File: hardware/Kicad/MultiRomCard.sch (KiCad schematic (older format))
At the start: 16 parts, among them P1 VC4000_Cartridge_Bus, U1 Arduino_UNO, U2 74HC595, U3 74HC595, U4 74HC595, U5 6264, U6 74HC245, U7 74HC245, U8 74HC245

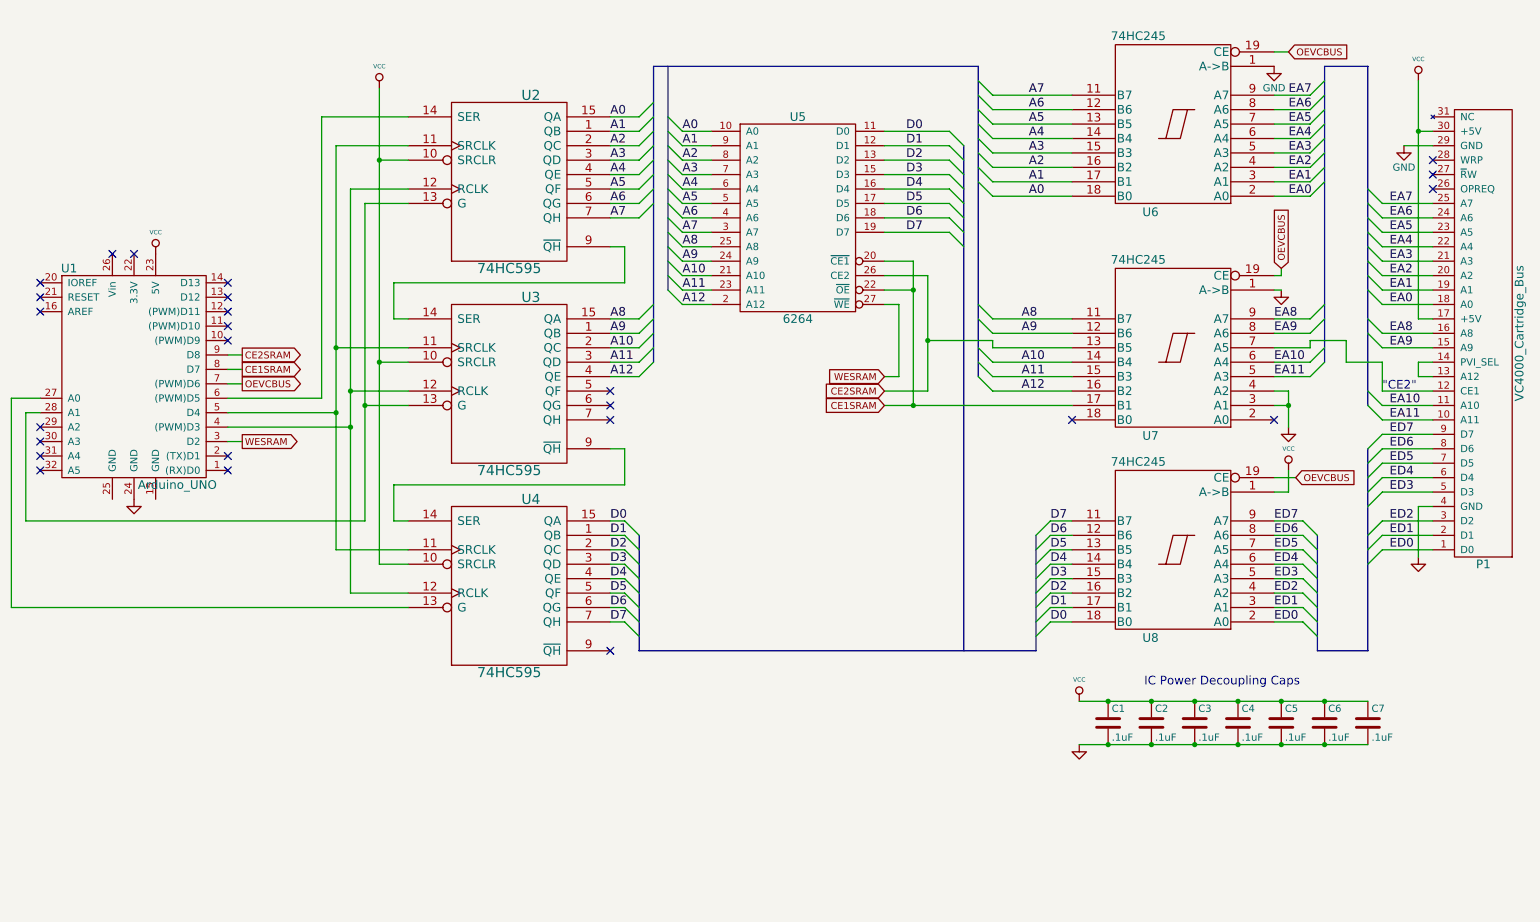
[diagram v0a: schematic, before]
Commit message: [SCH/PCB] Added and connected missing Arduino GND Pins.
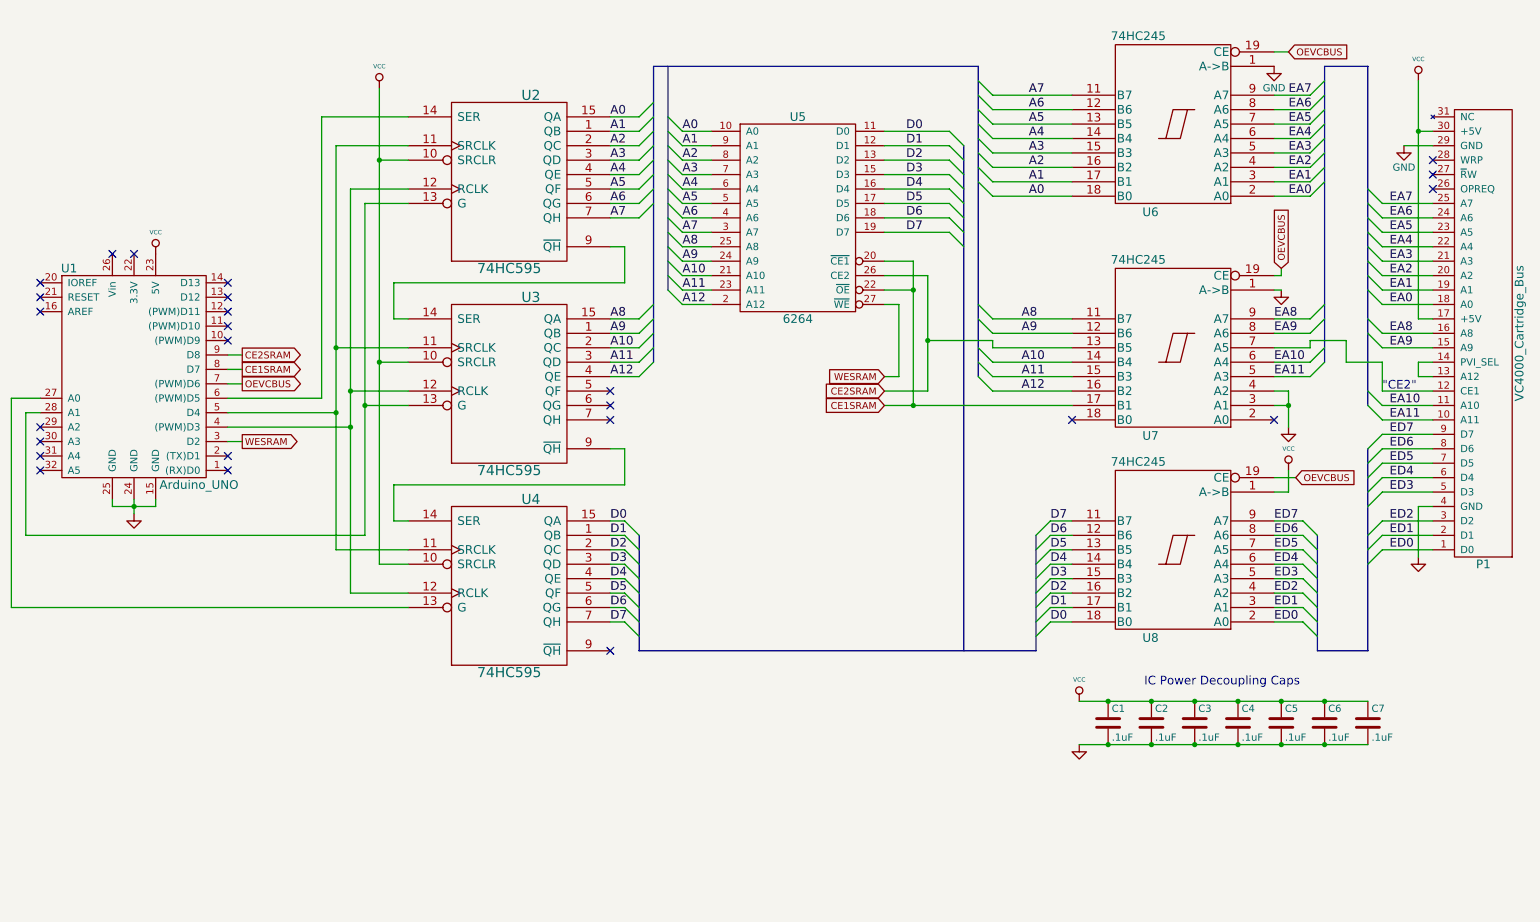
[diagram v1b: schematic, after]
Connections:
- net GND: now also U1.15 (GND), U1.25 (GND)

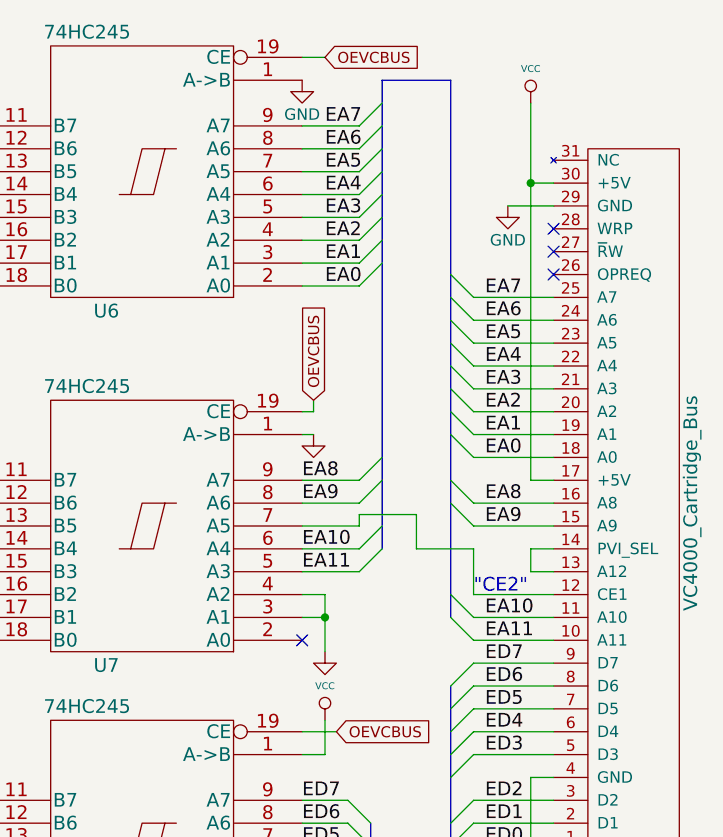
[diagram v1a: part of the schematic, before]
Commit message: [SCH/PCB] Cleaning up both schematic and PCB a bit.
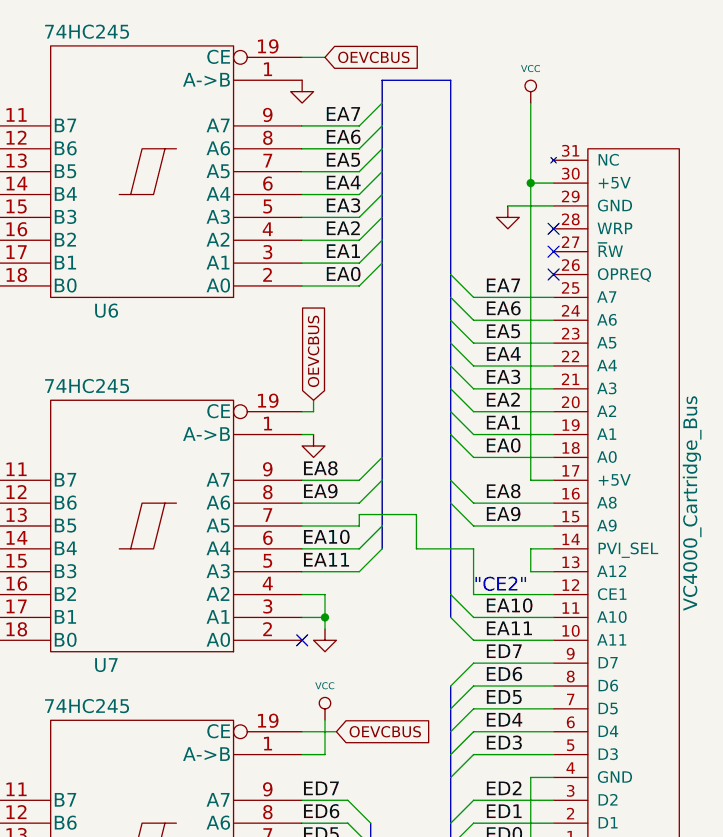
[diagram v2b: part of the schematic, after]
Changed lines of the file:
@@
 Sheet 1 1
 Title "Interton VC4000 MultiRom Cartridge"
-Date "Sunday, June 21, 2015"
+Date "Monday, June 22, 2015"
 Rev "0.1"
 Comp "Mario Keller and Johannes Maibaum"
@@
 L GND #PWR07
 U 1 1 54DB8BDD
-P 9550 4000
-F 0 "#PWR07" H 9550 4000 30  0001 C CNN
-F 1 "GND" H 9550 3930 30  0001 C CNN
-F 2 "" H 9550 4000 60  0000 C CNN
-F 3 "" H 9550 4000 60  0000 C CNN
-	1    9550 4000
+P 9550 3900
+F 0 "#PWR07" H 9550 3900 30  0001 C CNN
+F 1 "GND" H 9550 3830 30  0001 C CNN
+F 2 "" H 9550 3900 60  0000 C CNN
+F 3 "" H 9550 3900 60  0000 C CNN
+	1    9550 3900
 	1    0    0    -1
 $EndComp
@@
 Text Notes 10200 3750 0    60   ~ 0
 "CE2"
-$Comp
-L GND #PWR09
-U 1 1 553D09E4
-P 10350 2050
-F 0 "#PWR09" H 10350 1800 50  0001 C CNN
-F 1 "GND" H 10350 1900 50  0000 C CNN
-F 2 "" H 10350 2050 60  0000 C CNN
-F 3 "" H 10350 2050 60  0000 C CNN
-	1    10350 2050
-	1    0    0    -1
-$EndComp
-$Comp
-L GND #PWR010
-U 1 1 553D11BE
-P 9450 1500
-F 0 "#PWR010" H 9450 1250 50  0001 C CNN
-F 1 "GND" H 9450 1350 50  0000 C CNN
-F 2 "" H 9450 1500 60  0000 C CNN
-F 3 "" H 9450 1500 60  0000 C CNN
-	1    9450 1500
-	1    0    0    -1
-$EndComp
 Entry Wire Line
 	10100 4750 10200 4650
@@
 $EndComp
 $Comp
-L GND #PWR011
+L GND #PWR09
 U 1 1 558564D3
 P 8100 6200
-F 0 "#PWR011" H 8100 6200 30  0001 C CNN
+F 0 "#PWR09" H 8100 6200 30  0001 C CNN
 F 1 "GND" H 8100 6130 30  0001 C CNN
 F 2 "" H 8100 6200 60  0000 C CNN
@@
 $EndComp
 $Comp
-L VCC #PWR012
+L VCC #PWR010
 U 1 1 5585650E
 P 8100 5900
-F 0 "#PWR012" H 8100 6000 30  0001 C CNN
+F 0 "#PWR010" H 8100 6000 30  0001 C CNN
 F 1 "VCC" H 8100 6050 30  0000 C CNN
 F 2 "" H 8100 5900 60  0000 C CNN
@@
 	6750 3850 8050 3850
 Wire Wire Line
-	9550 3750 9550 4000
+	9550 3750 9550 3900
 Wire Wire Line
 	9550 3850 9450 3850
@@
 	1700 4550 1700 4500
 Connection ~ 1550 4550
+$Comp
+L GND #PWR011
+U 1 1 5587E073
+P 9450 1500
+F 0 "#PWR011" H 9450 1500 30  0001 C CNN
+F 1 "GND" H 9450 1430 30  0001 C CNN
+F 2 "" H 9450 1500 60  0000 C CNN
+F 3 "" H 9450 1500 60  0000 C CNN
+	1    9450 1500
+	1    0    0    -1
+$EndComp
+$Comp
+L GND #PWR012
+U 1 1 5587E24F
+P 10350 2050
+F 0 "#PWR012" H 10350 2050 30  0001 C CNN
+F 1 "GND" H 10350 1980 30  0001 C CNN
+F 2 "" H 10350 2050 60  0000 C CNN
+F 3 "" H 10350 2050 60  0000 C CNN
+	1    10350 2050
+	1    0    0    -1
+$EndComp
 $EndSCHEMATC

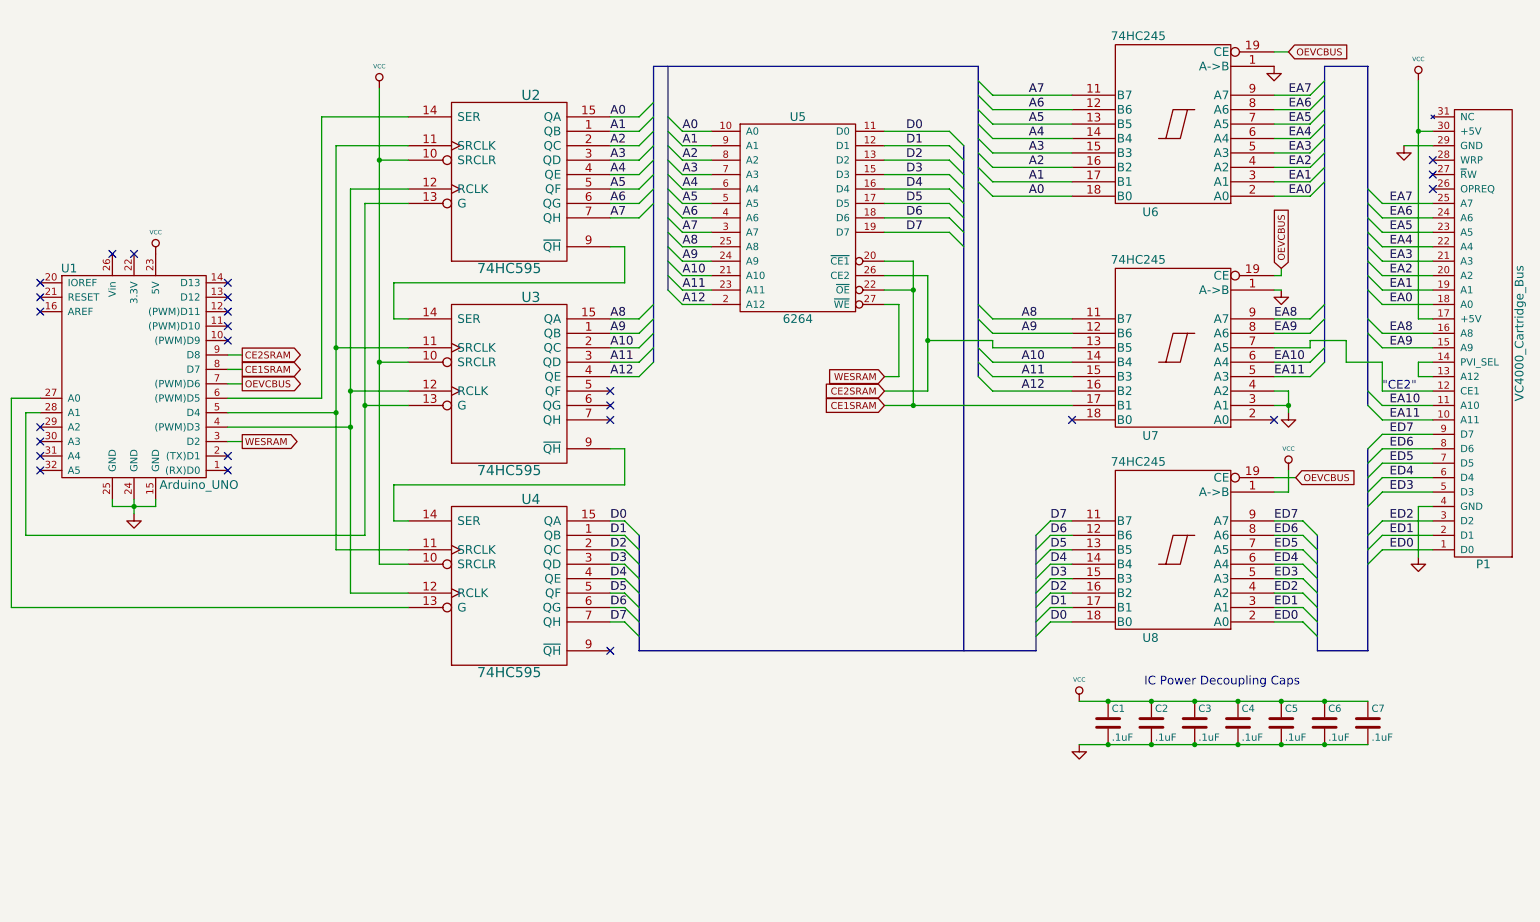
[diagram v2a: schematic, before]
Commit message: [SCH/PCB] Add Pin header for MicroSD Card Breakout Board.
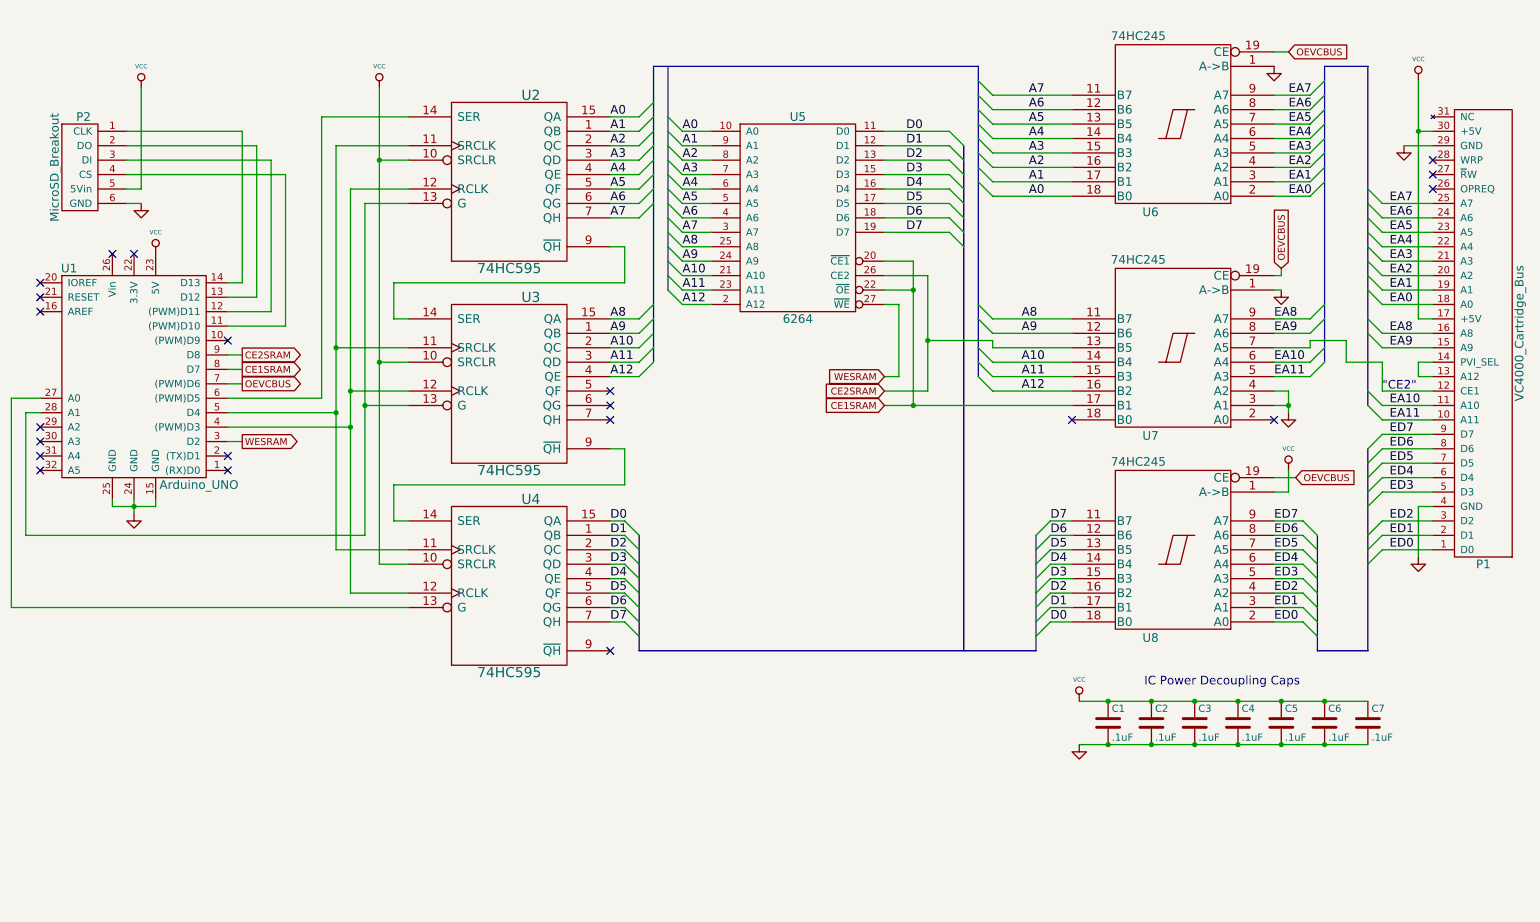
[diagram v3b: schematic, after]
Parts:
- added P2: MicroSD_Breakout, Pin_Headers:Pin_Header_Straight_1x06, symbol MicroSD_Breakout
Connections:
- net GND: now also P2.6 (GND)
- net VCC: now also P2.5 (5Vin)
- net at U1.11 ((PWM)D10): now also P2.4 (CS)
- net at U1.12 ((PWM)D11): now also P2.3 (DI)
- net at U1.13 (D12): now also P2.2 (DO)
- net at U1.14 (D13): now also P2.1 (CLK)
- no-connect marks 25 -> 21
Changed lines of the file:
@@
 NoConn ~ 2200 4300
 NoConn ~ 2200 4200
-NoConn ~ 2200 3400
-NoConn ~ 2200 3300
-NoConn ~ 2200 3200
-NoConn ~ 2200 3100
-NoConn ~ 2200 3000
 $Comp
 L VCC #PWR03
@@
 Text Notes 8550 5800 0    60   ~ 0
 IC Power Decoupling Caps
+$Comp
+L GND #PWR011
+U 1 1 5587E073
+P 9450 1500
+F 0 "#PWR011" H 9450 1500 30  0001 C CNN
+F 1 "GND" H 9450 1430 30  0001 C CNN
+F 2 "" H 9450 1500 60  0000 C CNN
+F 3 "" H 9450 1500 60  0000 C CNN
+	1    9450 1500
+	1    0    0    -1
+$EndComp
+$Comp
+L GND #PWR012
+U 1 1 5587E24F
+P 10350 2050
+F 0 "#PWR012" H 10350 2050 30  0001 C CNN
+F 1 "GND" H 10350 1980 30  0001 C CNN
+F 2 "" H 10350 2050 60  0000 C CNN
+F 3 "" H 10350 2050 60  0000 C CNN
+	1    10350 2050
+	1    0    0    -1
+$EndComp
+$Comp
+L GND #PWR013
+U 1 1 5587EA58
+P 1600 2450
+F 0 "#PWR013" H 1600 2450 30  0001 C CNN
+F 1 "GND" H 1600 2380 30  0001 C CNN
+F 2 "" H 1600 2450 60  0000 C CNN
+F 3 "" H 1600 2450 60  0000 C CNN
+	1    1600 2450
+	1    0    0    -1
+$EndComp
+NoConn ~ 2200 3400
 Wire Wire Line
 	4950 3000 3350 3000
@@
 	10450 3250 10550 3250
 Wire Bus Line
-	10100 5550 9750 5550
+	9750 5550 10100 5550
 Wire Wire Line
 	2200 3800 2850 3800
@@
 	9550 4450 9450 4450
 Wire Bus Line
-	10100 4150 10100 5550
+	10100 5550 10100 4150
 Wire Wire Line
 	9500 2950 9450 2950
@@
 	1700 4550 1700 4500
 Connection ~ 1550 4550
-$Comp
-L GND #PWR011
-U 1 1 5587E073
-P 9450 1500
-F 0 "#PWR011" H 9450 1500 30  0001 C CNN
-F 1 "GND" H 9450 1430 30  0001 C CNN
-F 2 "" H 9450 1500 60  0000 C CNN
-F 3 "" H 9450 1500 60  0000 C CNN
-	1    9450 1500
-	1    0    0    -1
-$EndComp
-$Comp
-L GND #PWR012
-U 1 1 5587E24F
-P 10350 2050
-F 0 "#PWR012" H 10350 2050 30  0001 C CNN
-F 1 "GND" H 10350 1980 30  0001 C CNN
-F 2 "" H 10350 2050 60  0000 C CNN
-F 3 "" H 10350 2050 60  0000 C CNN
-	1    10350 2050
-	1    0    0    -1
+Wire Wire Line
+	1500 2350 1600 2350
+Wire Wire Line
+	1600 2350 1600 1650
+Wire Wire Line
+	1500 2250 2600 2250
+Wire Wire Line
+	2600 2250 2600 3300
+Wire Wire Line
+	2600 3300 2200 3300
+Wire Wire Line
+	1500 1950 2300 1950
+Wire Wire Line
+	2300 1950 2300 3000
+Wire Wire Line
+	2300 3000 2200 3000
+Wire Wire Line
+	1500 2050 2400 2050
+Wire Wire Line
+	2400 2050 2400 3100
+Wire Wire Line
+	2400 3100 2200 3100
+Wire Wire Line
+	1500 2150 2500 2150
+Wire Wire Line
+	2500 2150 2500 3200
+Wire Wire Line
+	2500 3200 2200 3200
+Wire Wire Line
+	1500 2450 1600 2450
+$Comp
+L VCC #PWR014
+U 1 1 5587FD9D
+P 1600 1650
+F 0 "#PWR014" H 1600 1750 30  0001 C CNN
+F 1 "VCC" H 1600 1800 30  0000 C CNN
+F 2 "" H 1600 1650 60  0000 C CNN
+F 3 "" H 1600 1650 60  0000 C CNN
+	1    1600 1650
+	1    0    0    -1
+$EndComp
+$Comp
+L MicroSD_Breakout P2
+U 1 1 55880347
+P 1300 2200
+F 0 "P2" H 1400 2550 60  0000 C CNN
+F 1 "MicroSD_Breakout" V 1600 2200 60  0000 C CNN
+F 2 "Pin_Headers:Pin_Header_Straight_1x06" H 1300 2200 60  0001 C CNN
+F 3 "" H 1300 2200 60  0000 C CNN
+	1    1300 2200
+	-1   0    0    -1
 $EndComp
 $EndSCHEMATC
